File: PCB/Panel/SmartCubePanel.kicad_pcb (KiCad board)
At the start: 2 copper layers, 174.6 x 142.8 mm, 912 parts, among them J1 PogoPinPad, J1 SWD_Programmer, J1 Shield_Connector_Top_Left, J2 Conn_01x06, J2 Shield_Connector_Bottom_Left, J2 Shield_Connector_Top_Right, J3 PogoPinPad, J3 Shield_Connector_Bottom_Right, J3 Shield_Connector_Top_Right, J4 PogoPinPad, J4 Shield_Connector_Bottom_Right, J4 Shield_Connector_Top_Left, J5 Shield_Connector_Bottom_Left, U1 HallLinearSensor, U1 PY32F002BF15P6TU, U1 PogoPin, U2 PinHeaderTop, U2 PogoPin, U3 PinHeaderRight, U3 PogoPin, U4 PinHeaderBottom, U5 PinHeaderLeft

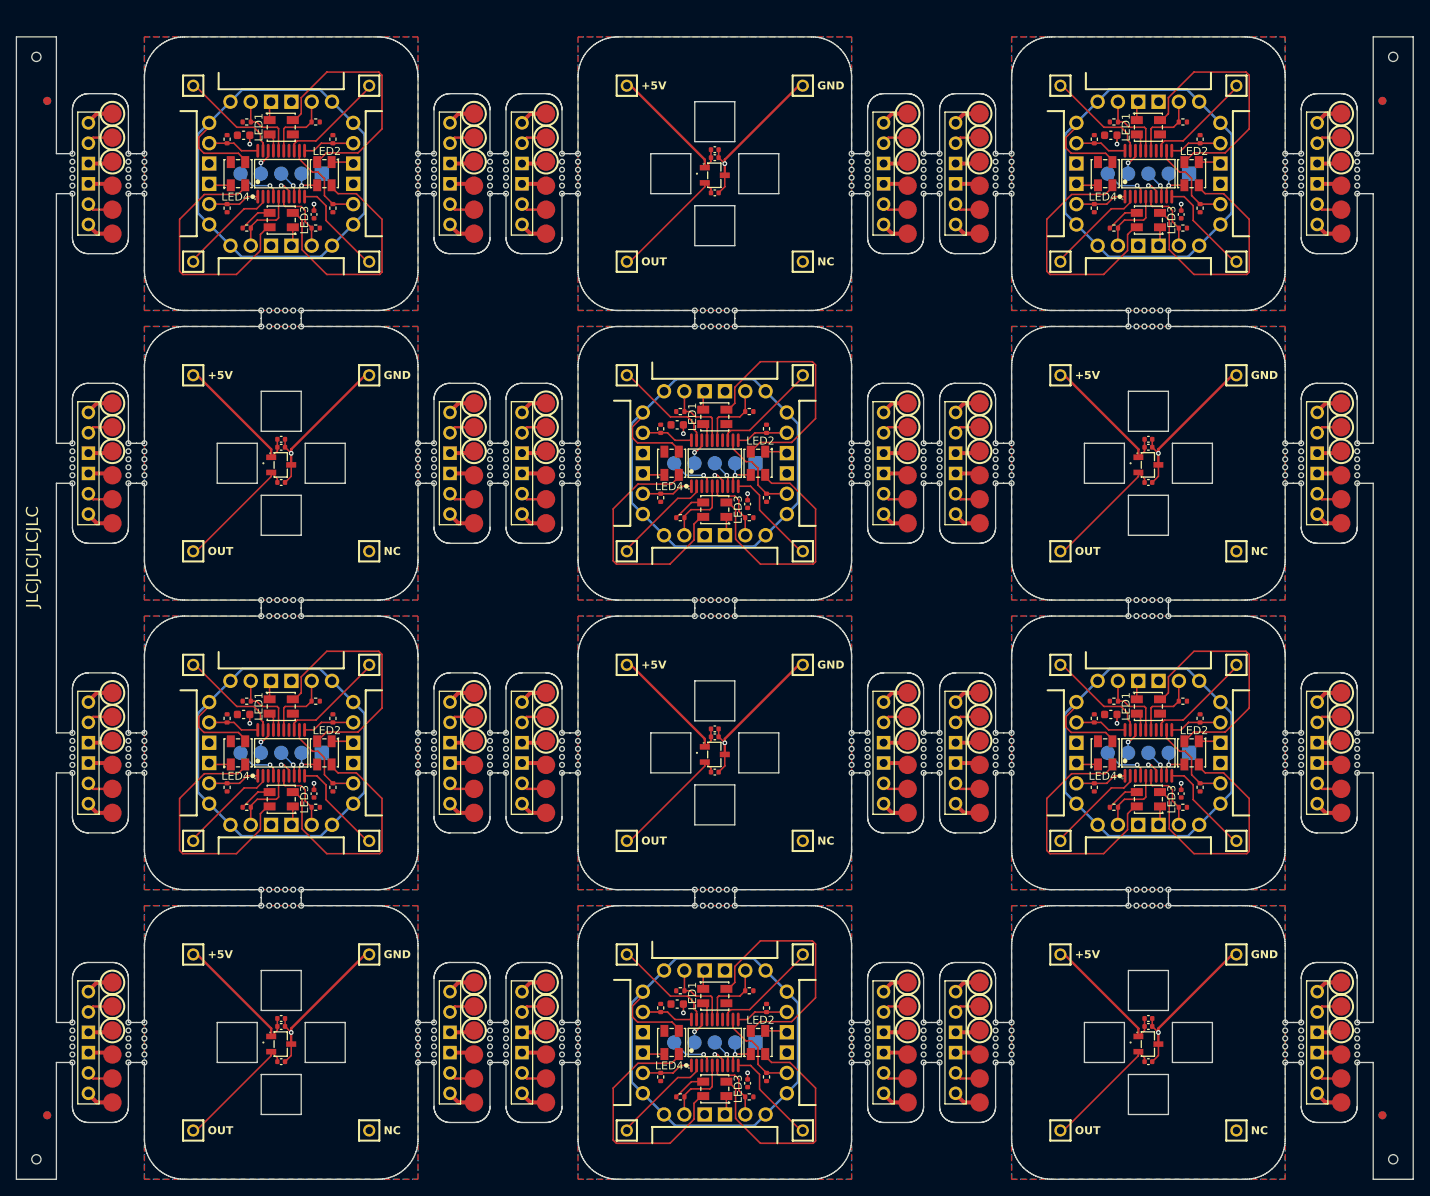
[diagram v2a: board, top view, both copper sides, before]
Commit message: Finish module, power supply and connector design, panel is wip
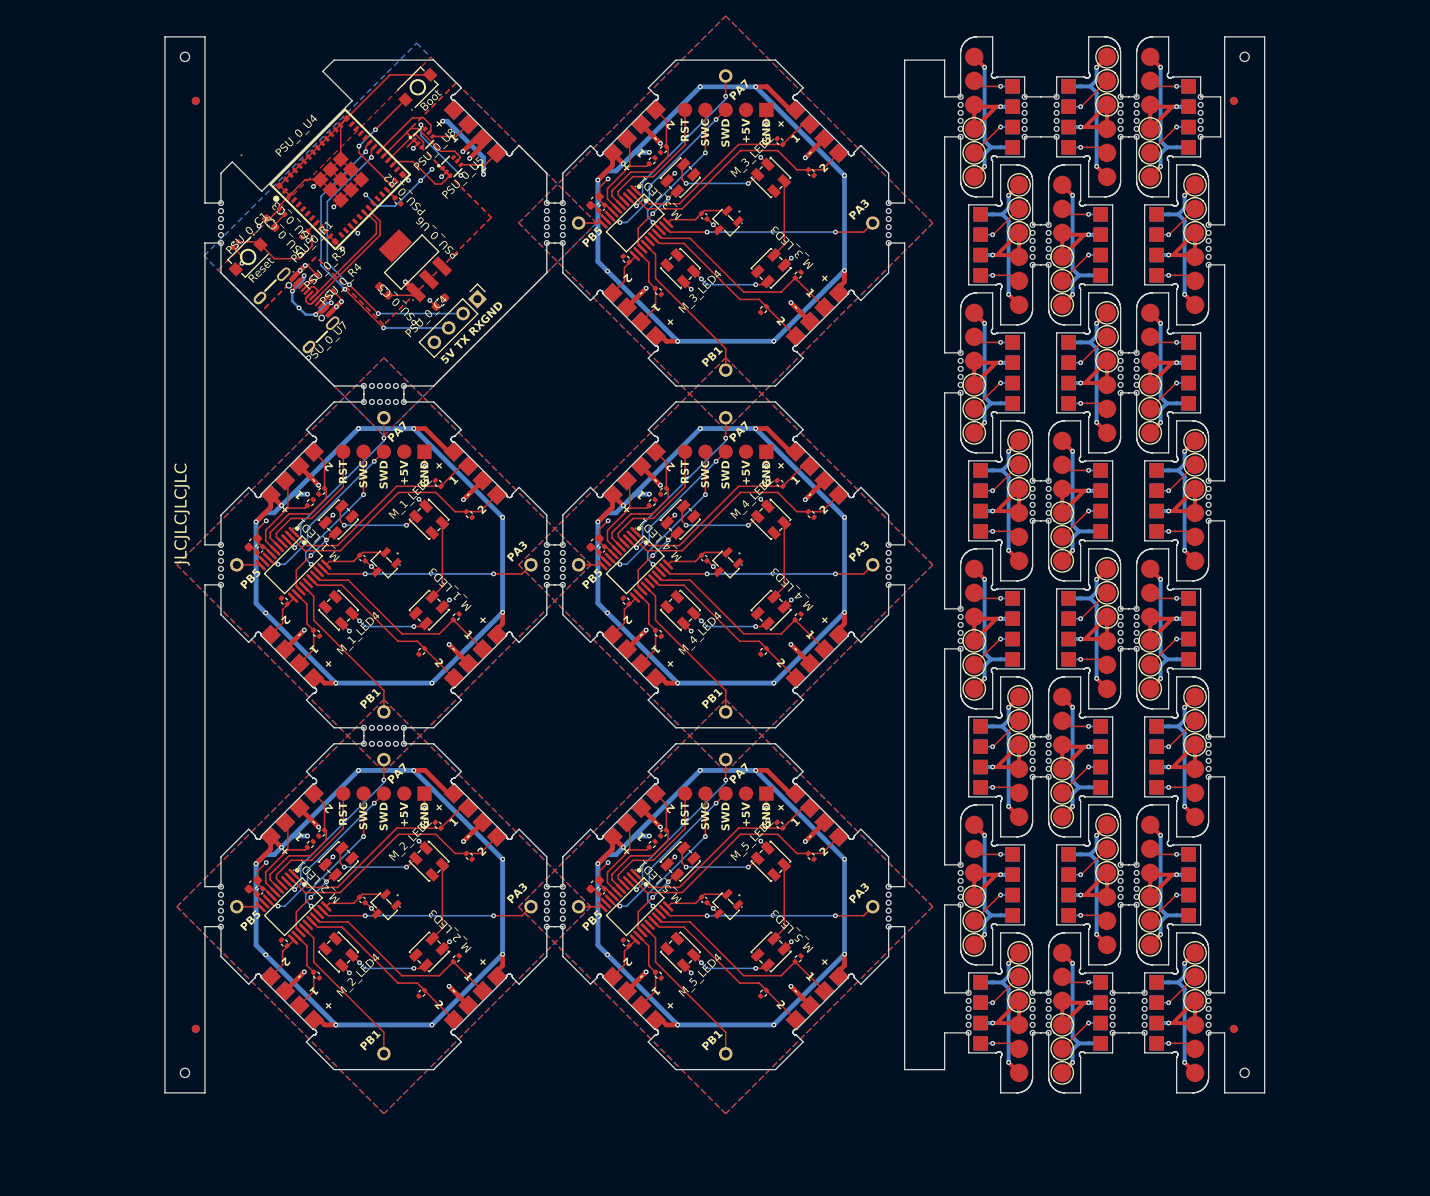
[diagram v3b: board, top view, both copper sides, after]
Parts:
- removed C1 (x6): 10nF, Capacitor_SMD:C_0402_1005Metric
- removed C1 (x6): 10uF, Capacitor_SMD:C_0603_1608Metric
- removed C2 (x6), C3 (x6): 1nF, Capacitor_SMD:C_0402_1005Metric
- removed C2 (x6): 100nF, Capacitor_SMD:C_0402_1005Metric
- removed J1 (x24), J3 (x24), J4 (x24): PogoPinPad, CustomFootprints:PogoPinPad
- removed J1 (x6), J4 (x6): Shield_Connector_Top_Left, CustomFootprints:HDR-TH_1P-V-F-1
- removed J1 (x6): SWD_Programmer, CustomFootprints:SWD_Pad
- removed J2 (x24): Conn_01x06, CustomFootprints:Connector_PinHeader_2.54mm_Vertical
- removed J2 (x6), J5 (x6): Shield_Connector_Bottom_Left, CustomFootprints:HDR-TH_1P-V-F-1
- removed J2 (x6), J3 (x6): Shield_Connector_Top_Right, CustomFootprints:HDR-TH_1P-V-F-1
- removed J3 (x6), J4 (x6): Shield_Connector_Bottom_Right, CustomFootprints:HDR-TH_1P-V-F-1
- removed KiKit_MB_47_1, KiKit_MB_47_2, KiKit_MB_47_3, KiKit_MB_47_4, KiKit_MB_47_5, KiKit_MB_47_6, KiKit_MB_48_1, KiKit_MB_48_2, KiKit_MB_48_3, KiKit_MB_48_4, KiKit_MB_48_5, KiKit_MB_48_6, KiKit_MB_49_1, KiKit_MB_49_2, KiKit_MB_49_3, KiKit_MB_49_4, KiKit_MB_49_5, KiKit_MB_49_6, KiKit_MB_50_1, KiKit_MB_50_2, KiKit_MB_50_3, KiKit_MB_50_4, KiKit_MB_50_5, KiKit_MB_50_6, KiKit_MB_51_1, KiKit_MB_51_2, KiKit_MB_51_3, KiKit_MB_51_4, KiKit_MB_51_5, KiKit_MB_51_6, KiKit_MB_52_1, KiKit_MB_52_2, KiKit_MB_52_3, KiKit_MB_52_4, KiKit_MB_52_5, KiKit_MB_52_6, KiKit_MB_53_1, KiKit_MB_53_2, KiKit_MB_53_3, KiKit_MB_53_4, KiKit_MB_53_5, KiKit_MB_53_6, KiKit_MB_54_1, KiKit_MB_54_2, KiKit_MB_54_3, KiKit_MB_54_4, KiKit_MB_54_5, KiKit_MB_54_6, KiKit_MB_55_1, KiKit_MB_55_2, KiKit_MB_55_3, KiKit_MB_55_4, KiKit_MB_55_5, KiKit_MB_55_6, KiKit_MB_56_1, KiKit_MB_56_2, KiKit_MB_56_3, KiKit_MB_56_4, KiKit_MB_56_5, KiKit_MB_56_6, KiKit_MB_57_1, KiKit_MB_57_2, KiKit_MB_57_3, KiKit_MB_57_4, KiKit_MB_57_5, KiKit_MB_57_6, KiKit_MB_58_1, KiKit_MB_58_2, KiKit_MB_58_3, KiKit_MB_58_4, KiKit_MB_58_5, KiKit_MB_58_6, KiKit_MB_59_1, KiKit_MB_59_2, KiKit_MB_59_3, KiKit_MB_59_4, KiKit_MB_59_5, KiKit_MB_59_6, KiKit_MB_60_1, KiKit_MB_60_2, KiKit_MB_60_3, KiKit_MB_60_4, KiKit_MB_60_5, KiKit_MB_60_6, KiKit_MB_61_1, KiKit_MB_61_2, KiKit_MB_61_3, KiKit_MB_61_4, KiKit_MB_61_5, KiKit_MB_61_6, KiKit_MB_62_1, KiKit_MB_62_2, KiKit_MB_62_3, KiKit_MB_62_4, KiKit_MB_62_5, KiKit_MB_62_6, KiKit_MB_63_1, KiKit_MB_63_2, KiKit_MB_63_3, KiKit_MB_63_4, KiKit_MB_63_5, KiKit_MB_63_6, KiKit_MB_64_1, KiKit_MB_64_2, KiKit_MB_64_3, KiKit_MB_64_4, KiKit_MB_64_5, KiKit_MB_64_6, KiKit_MB_65_1, KiKit_MB_65_2, KiKit_MB_65_3, KiKit_MB_65_4, KiKit_MB_65_5, KiKit_MB_65_6, KiKit_MB_66_1, KiKit_MB_66_2, KiKit_MB_66_3, KiKit_MB_66_4, KiKit_MB_66_5, KiKit_MB_66_6, KiKit_MB_67_1, KiKit_MB_67_2, KiKit_MB_67_3, KiKit_MB_67_4, KiKit_MB_67_5, KiKit_MB_67_6, KiKit_MB_68_1, KiKit_MB_68_2, KiKit_MB_68_3, KiKit_MB_68_4, KiKit_MB_68_5, KiKit_MB_68_6, KiKit_MB_69_1, KiKit_MB_69_2, KiKit_MB_69_3, KiKit_MB_69_4, KiKit_MB_69_5, KiKit_MB_69_6, KiKit_MB_70_1, KiKit_MB_70_2, KiKit_MB_70_3, KiKit_MB_70_4, KiKit_MB_70_5, KiKit_MB_70_6, KiKit_MB_71_1, KiKit_MB_71_2, KiKit_MB_71_3, KiKit_MB_71_4, KiKit_MB_71_5, KiKit_MB_71_6, KiKit_MB_72_1, KiKit_MB_72_2, KiKit_MB_72_3, KiKit_MB_72_4, KiKit_MB_72_5, KiKit_MB_72_6, KiKit_MB_73_1, KiKit_MB_73_2, KiKit_MB_73_3, KiKit_MB_73_4, KiKit_MB_73_5, KiKit_MB_73_6, KiKit_MB_74_1, KiKit_MB_74_2, KiKit_MB_74_3, KiKit_MB_74_4, KiKit_MB_74_5, KiKit_MB_74_6, KiKit_MB_75_1, KiKit_MB_75_2, KiKit_MB_75_3, KiKit_MB_75_4, KiKit_MB_75_5, KiKit_MB_75_6, KiKit_MB_76_1, KiKit_MB_76_2, KiKit_MB_76_3, KiKit_MB_76_4, KiKit_MB_76_5, KiKit_MB_76_6, KiKit_MB_77_1, KiKit_MB_77_2, KiKit_MB_77_3, KiKit_MB_77_4, KiKit_MB_77_5, KiKit_MB_77_6, KiKit_MB_78_1, KiKit_MB_78_2, KiKit_MB_78_3, KiKit_MB_78_4, KiKit_MB_78_5, KiKit_MB_78_6, KiKit_MB_79_1, KiKit_MB_79_2, KiKit_MB_79_3, KiKit_MB_79_4, KiKit_MB_79_5, KiKit_MB_79_6, KiKit_MB_80_1, KiKit_MB_80_2, KiKit_MB_80_3, KiKit_MB_80_4, KiKit_MB_80_5, KiKit_MB_80_6, KiKit_MB_81_1, KiKit_MB_81_2, KiKit_MB_81_3, KiKit_MB_81_4, KiKit_MB_81_5, KiKit_MB_81_6, KiKit_MB_82_1, KiKit_MB_82_2, KiKit_MB_82_3, KiKit_MB_82_4, KiKit_MB_82_5, KiKit_MB_82_6, KiKit_MB_83_1, KiKit_MB_83_2, KiKit_MB_83_3, KiKit_MB_83_4, KiKit_MB_83_5, KiKit_MB_83_6, KiKit_MB_84_1, KiKit_MB_84_2, KiKit_MB_84_3, KiKit_MB_84_4, KiKit_MB_84_5, KiKit_MB_84_6, KiKit_MB_85_1, KiKit_MB_85_2, KiKit_MB_85_3, KiKit_MB_85_4, KiKit_MB_85_5, KiKit_MB_85_6, KiKit_MB_86_1, KiKit_MB_86_2, KiKit_MB_86_3, KiKit_MB_86_4, KiKit_MB_86_5, KiKit_MB_86_6, KiKit_MB_87_1, KiKit_MB_87_2, KiKit_MB_87_3, KiKit_MB_87_4, KiKit_MB_87_5, KiKit_MB_87_6, KiKit_MB_88_1, KiKit_MB_88_2, KiKit_MB_88_3, KiKit_MB_88_4, KiKit_MB_88_5, KiKit_MB_88_6, KiKit_MB_89_1, KiKit_MB_89_2, KiKit_MB_89_3, KiKit_MB_89_4, KiKit_MB_89_5, KiKit_MB_89_6, KiKit_MB_90_1, KiKit_MB_90_2, KiKit_MB_90_3, KiKit_MB_90_4, KiKit_MB_90_5, KiKit_MB_90_6: NPTH, NPTH
- removed LED1 (x6), LED2 (x6), LED3 (x6), LED4 (x6): SK6812MINI-HS, CustomFootprints:LED-SK6812MINI-HS
- removed R1 (x6), R2 (x6), R3 (x6), R4 (x6), R5 (x6), R6 (x6), R7 (x6), R8 (x6): 10k, Resistor_SMD:R_0402_1005Metric
- removed U1 (x6): PY32F002BF15P6TU, CustomFootprints:Py32
- removed U1 (x24), U2 (x24), U3 (x24): PogoPin, CustomFootprints:PogoPin
- removed U1 (x6): HallLinearSensor, CustomFootprints:HallLinearSensor
- removed U2 (x6): PinHeaderTop, CustomFootprints:01x06_PinHeader_Angled
- removed U3 (x6): PinHeaderRight, CustomFootprints:01x06_PinHeader_Angled
- removed U4 (x6): PinHeaderBottom, CustomFootprints:01x06_PinHeader_Angled
- removed U5 (x6): PinHeaderLeft, CustomFootprints:01x06_PinHeader_Angled
- added M_1_C1: 10uF, Capacitor_SMD:C_0603_1608Metric, F.Cu at (90.8, 83.2)
- added M_1_C2: 100nF, Capacitor_SMD:C_0402_1005Metric, F.Cu at (91.6, 84.1)
- added M_1_C3: 10nF, Capacitor_SMD:C_0402_1005Metric, F.Cu at (104.4, 85.2)
- added M_1_J1: SWD_Programmer, CustomFootprints:SWD_Pad, F.Cu at (107.2, 71.9)
- added M_1_J2: Conn_01x01, CustomFootprints:ShieldConnector, F.Cu at (88.6, 86.1)
- added M_1_J3: Conn_01x01, CustomFootprints:ShieldConnector, F.Cu at (107.0, 104.5)
- added M_1_J4: Conn_01x01, CustomFootprints:ShieldConnector, F.Cu at (107.0, 67.8)
- added M_1_J5: Conn_01x01, CustomFootprints:ShieldConnector, F.Cu at (125.4, 86.1)
- added M_1_LED1: SK6812MINI-HS, CustomFootprints:LED-SK6812MINI-HS, F.Cu at (101.5, 80.3)
- added M_1_LED2: SK6812MINI-HS, CustomFootprints:LED-SK6812MINI-HS, F.Cu at (112.8, 80.3)
- added M_1_LED3: SK6812MINI-HS, CustomFootprints:LED-SK6812MINI-HS, F.Cu at (112.8, 91.7)
- added M_1_LED4: SK6812MINI-HS, CustomFootprints:LED-SK6812MINI-HS, F.Cu at (101.5, 91.7)
- added M_1_PinHeaderBottom1: PinHeader, CustomFootprints:01x04_PinPads, F.Cu at (118.6, 97.5)
- added M_1_PinHeaderLeft1: PinHeader, CustomFootprints:01x04_PinPads, F.Cu at (95.7, 97.5)
- added M_1_PinHeaderRight1: PinHeader, CustomFootprints:01x04_PinPads, F.Cu at (118.6, 74.5)
- added M_1_PinHeaderTop1: PinHeader, CustomFootprints:01x04_PinPads, F.Cu at (95.7, 74.5)
- added M_1_R1: 10k, Resistor_SMD:R_0402_1005Metric, F.Cu at (99.4, 76.8)
- added M_1_R2: 10k, Resistor_SMD:R_0402_1005Metric, F.Cu at (97.9, 78.2)
- added M_1_R3: 10k, Resistor_SMD:R_0402_1005Metric, F.Cu at (117.8, 79.7)
- added M_1_R4: 10k, Resistor_SMD:R_0402_1005Metric, F.Cu at (113.9, 75.8)
- added M_1_R5: 10k, Resistor_SMD:R_0402_1005Metric, F.Cu at (111.9, 96.8)
- added M_1_R6: 10k, Resistor_SMD:R_0402_1005Metric, F.Cu at (116.2, 92.5)
- added M_1_R7: 10k, Resistor_SMD:R_0402_1005Metric, F.Cu at (94.7, 90.5)
- added M_1_R8: 10k, Resistor_SMD:R_0402_1005Metric, F.Cu at (98.7, 94.6)
- added M_1_U1: PY32F002BF15P6TU, CustomFootprints:Py32, F.Cu at (95.8, 86.0)
- added M_1_U6: HallLinearSensor, CustomFootprints:HallLinearSensor, F.Cu at (107.1, 86.0)
- added M_2_C1: 10uF, Capacitor_SMD:C_0603_1608Metric, F.Cu at (90.8, 126.0)
- added M_2_C2: 100nF, Capacitor_SMD:C_0402_1005Metric, F.Cu at (91.6, 126.8)
- added M_2_C3: 10nF, Capacitor_SMD:C_0402_1005Metric, F.Cu at (104.4, 127.9)
- added M_2_J1: SWD_Programmer, CustomFootprints:SWD_Pad, F.Cu at (107.2, 114.6)
- added M_2_J2: Conn_01x01, CustomFootprints:ShieldConnector, F.Cu at (88.6, 128.9)
- added M_2_J3: Conn_01x01, CustomFootprints:ShieldConnector, F.Cu at (107.0, 147.3)
- added M_2_J4: Conn_01x01, CustomFootprints:ShieldConnector, F.Cu at (107.0, 110.5)
- added M_2_J5: Conn_01x01, CustomFootprints:ShieldConnector, F.Cu at (125.4, 128.9)
- added M_2_LED1: SK6812MINI-HS, CustomFootprints:LED-SK6812MINI-HS, F.Cu at (101.5, 123.1)
- added M_2_LED2: SK6812MINI-HS, CustomFootprints:LED-SK6812MINI-HS, F.Cu at (112.8, 123.1)
- added M_2_LED3: SK6812MINI-HS, CustomFootprints:LED-SK6812MINI-HS, F.Cu at (112.8, 134.4)
- added M_2_LED4: SK6812MINI-HS, CustomFootprints:LED-SK6812MINI-HS, F.Cu at (101.5, 134.4)
- added M_2_PinHeaderBottom1: PinHeader, CustomFootprints:01x04_PinPads, F.Cu at (118.6, 140.2)
- added M_2_PinHeaderLeft1: PinHeader, CustomFootprints:01x04_PinPads, F.Cu at (95.7, 140.2)
- added M_2_PinHeaderRight1: PinHeader, CustomFootprints:01x04_PinPads, F.Cu at (118.6, 117.3)
- added M_2_PinHeaderTop1: PinHeader, CustomFootprints:01x04_PinPads, F.Cu at (95.7, 117.3)
- added M_2_R1: 10k, Resistor_SMD:R_0402_1005Metric, F.Cu at (99.4, 119.5)
- added M_2_R2: 10k, Resistor_SMD:R_0402_1005Metric, F.Cu at (97.9, 121.0)
- added M_2_R3: 10k, Resistor_SMD:R_0402_1005Metric, F.Cu at (117.8, 122.4)
- added M_2_R4: 10k, Resistor_SMD:R_0402_1005Metric, F.Cu at (113.9, 118.5)
- added M_2_R5: 10k, Resistor_SMD:R_0402_1005Metric, F.Cu at (111.9, 139.5)
- added M_2_R6: 10k, Resistor_SMD:R_0402_1005Metric, F.Cu at (116.2, 135.2)
- added M_2_R7: 10k, Resistor_SMD:R_0402_1005Metric, F.Cu at (94.7, 133.3)
- added M_2_R8: 10k, Resistor_SMD:R_0402_1005Metric, F.Cu at (98.7, 137.3)
- added M_2_U1: PY32F002BF15P6TU, CustomFootprints:Py32, F.Cu at (95.8, 128.7)
- added M_2_U6: HallLinearSensor, CustomFootprints:HallLinearSensor, F.Cu at (107.1, 128.7)
- added M_3_C1: 10uF, Capacitor_SMD:C_0603_1608Metric, F.Cu at (133.5, 40.5)
- added M_3_C2: 100nF, Capacitor_SMD:C_0402_1005Metric, F.Cu at (134.4, 41.4)
- added M_3_C3: 10nF, Capacitor_SMD:C_0402_1005Metric, F.Cu at (147.2, 42.4)
- added M_3_J1: SWD_Programmer, CustomFootprints:SWD_Pad, F.Cu at (149.9, 29.1)
- added M_3_J2: Conn_01x01, CustomFootprints:ShieldConnector, F.Cu at (131.3, 43.4)
- added M_3_J3: Conn_01x01, CustomFootprints:ShieldConnector, F.Cu at (149.7, 61.8)
- added M_3_J4: Conn_01x01, CustomFootprints:ShieldConnector, F.Cu at (149.7, 25.0)
- added M_3_J5: Conn_01x01, CustomFootprints:ShieldConnector, F.Cu at (168.1, 43.4)
- added M_3_LED1: SK6812MINI-HS, CustomFootprints:LED-SK6812MINI-HS, F.Cu at (144.2, 37.6)
- added M_3_LED2: SK6812MINI-HS, CustomFootprints:LED-SK6812MINI-HS, F.Cu at (155.5, 37.6)
- added M_3_LED3: SK6812MINI-HS, CustomFootprints:LED-SK6812MINI-HS, F.Cu at (155.5, 48.9)
- added M_3_LED4: SK6812MINI-HS, CustomFootprints:LED-SK6812MINI-HS, F.Cu at (144.2, 48.9)
- added M_3_PinHeaderBottom1: PinHeader, CustomFootprints:01x04_PinPads, F.Cu at (161.3, 54.7)
- added M_3_PinHeaderLeft1: PinHeader, CustomFootprints:01x04_PinPads, F.Cu at (138.4, 54.7)
- added M_3_PinHeaderRight1: PinHeader, CustomFootprints:01x04_PinPads, F.Cu at (161.3, 31.8)
- added M_3_PinHeaderTop1: PinHeader, CustomFootprints:01x04_PinPads, F.Cu at (138.4, 31.8)
- added M_3_R1: 10k, Resistor_SMD:R_0402_1005Metric, F.Cu at (142.1, 34.1)
- added M_3_R2: 10k, Resistor_SMD:R_0402_1005Metric, F.Cu at (140.7, 35.5)
- added M_3_R3: 10k, Resistor_SMD:R_0402_1005Metric, F.Cu at (160.5, 37.0)
- added M_3_R4: 10k, Resistor_SMD:R_0402_1005Metric, F.Cu at (156.7, 33.1)
- added M_3_R5: 10k, Resistor_SMD:R_0402_1005Metric, F.Cu at (154.6, 54.1)
- added M_3_R6: 10k, Resistor_SMD:R_0402_1005Metric, F.Cu at (158.9, 49.8)
- added M_3_R7: 10k, Resistor_SMD:R_0402_1005Metric, F.Cu at (137.4, 47.8)
- added M_3_R8: 10k, Resistor_SMD:R_0402_1005Metric, F.Cu at (141.5, 51.8)
- added M_3_U1: PY32F002BF15P6TU, CustomFootprints:Py32, F.Cu at (138.6, 43.3)
- added M_3_U6: HallLinearSensor, CustomFootprints:HallLinearSensor, F.Cu at (149.9, 43.3)
- added M_4_C1: 10uF, Capacitor_SMD:C_0603_1608Metric, F.Cu at (133.5, 83.2)
- added M_4_C2: 100nF, Capacitor_SMD:C_0402_1005Metric, F.Cu at (134.4, 84.1)
- added M_4_C3: 10nF, Capacitor_SMD:C_0402_1005Metric, F.Cu at (147.2, 85.2)
- added M_4_J1: SWD_Programmer, CustomFootprints:SWD_Pad, F.Cu at (149.9, 71.9)
- added M_4_J2: Conn_01x01, CustomFootprints:ShieldConnector, F.Cu at (131.3, 86.1)
- added M_4_J3: Conn_01x01, CustomFootprints:ShieldConnector, F.Cu at (149.7, 104.5)
- added M_4_J4: Conn_01x01, CustomFootprints:ShieldConnector, F.Cu at (149.7, 67.8)
- added M_4_J5: Conn_01x01, CustomFootprints:ShieldConnector, F.Cu at (168.1, 86.1)
- added M_4_LED1: SK6812MINI-HS, CustomFootprints:LED-SK6812MINI-HS, F.Cu at (144.2, 80.3)
- added M_4_LED2: SK6812MINI-HS, CustomFootprints:LED-SK6812MINI-HS, F.Cu at (155.5, 80.3)
- added M_4_LED3: SK6812MINI-HS, CustomFootprints:LED-SK6812MINI-HS, F.Cu at (155.5, 91.7)
- added M_4_LED4: SK6812MINI-HS, CustomFootprints:LED-SK6812MINI-HS, F.Cu at (144.2, 91.7)
- added M_4_PinHeaderBottom1: PinHeader, CustomFootprints:01x04_PinPads, F.Cu at (161.3, 97.5)
- added M_4_PinHeaderLeft1: PinHeader, CustomFootprints:01x04_PinPads, F.Cu at (138.4, 97.5)
- added M_4_PinHeaderRight1: PinHeader, CustomFootprints:01x04_PinPads, F.Cu at (161.3, 74.5)
- added M_4_PinHeaderTop1: PinHeader, CustomFootprints:01x04_PinPads, F.Cu at (138.4, 74.5)
- added M_4_R1: 10k, Resistor_SMD:R_0402_1005Metric, F.Cu at (142.1, 76.8)
- added M_4_R2: 10k, Resistor_SMD:R_0402_1005Metric, F.Cu at (140.7, 78.2)
- added M_4_R3: 10k, Resistor_SMD:R_0402_1005Metric, F.Cu at (160.5, 79.7)
- added M_4_R4: 10k, Resistor_SMD:R_0402_1005Metric, F.Cu at (156.7, 75.8)
- added M_4_R5: 10k, Resistor_SMD:R_0402_1005Metric, F.Cu at (154.6, 96.8)
- added M_4_R6: 10k, Resistor_SMD:R_0402_1005Metric, F.Cu at (158.9, 92.5)
- added M_4_R7: 10k, Resistor_SMD:R_0402_1005Metric, F.Cu at (137.4, 90.5)
- added M_4_R8: 10k, Resistor_SMD:R_0402_1005Metric, F.Cu at (141.5, 94.6)
- added M_4_U1: PY32F002BF15P6TU, CustomFootprints:Py32, F.Cu at (138.6, 86.0)
- added M_4_U6: HallLinearSensor, CustomFootprints:HallLinearSensor, F.Cu at (149.9, 86.0)
- added M_5_C1: 10uF, Capacitor_SMD:C_0603_1608Metric, F.Cu at (133.5, 126.0)
- added M_5_C2: 100nF, Capacitor_SMD:C_0402_1005Metric, F.Cu at (134.4, 126.8)
- added M_5_C3: 10nF, Capacitor_SMD:C_0402_1005Metric, F.Cu at (147.2, 127.9)
- added M_5_J1: SWD_Programmer, CustomFootprints:SWD_Pad, F.Cu at (149.9, 114.6)
- added M_5_J2: Conn_01x01, CustomFootprints:ShieldConnector, F.Cu at (131.3, 128.9)
- added M_5_J3: Conn_01x01, CustomFootprints:ShieldConnector, F.Cu at (149.7, 147.3)
- added M_5_J4: Conn_01x01, CustomFootprints:ShieldConnector, F.Cu at (149.7, 110.5)
- added M_5_J5: Conn_01x01, CustomFootprints:ShieldConnector, F.Cu at (168.1, 128.9)
- added M_5_LED1: SK6812MINI-HS, CustomFootprints:LED-SK6812MINI-HS, F.Cu at (144.2, 123.1)
- added M_5_LED2: SK6812MINI-HS, CustomFootprints:LED-SK6812MINI-HS, F.Cu at (155.5, 123.1)
- added M_5_LED3: SK6812MINI-HS, CustomFootprints:LED-SK6812MINI-HS, F.Cu at (155.5, 134.4)
- added M_5_LED4: SK6812MINI-HS, CustomFootprints:LED-SK6812MINI-HS, F.Cu at (144.2, 134.4)
- added M_5_PinHeaderBottom1: PinHeader, CustomFootprints:01x04_PinPads, F.Cu at (161.3, 140.2)
- added M_5_PinHeaderLeft1: PinHeader, CustomFootprints:01x04_PinPads, F.Cu at (138.4, 140.2)
- added M_5_PinHeaderRight1: PinHeader, CustomFootprints:01x04_PinPads, F.Cu at (161.3, 117.3)
- added M_5_PinHeaderTop1: PinHeader, CustomFootprints:01x04_PinPads, F.Cu at (138.4, 117.3)
- added M_5_R1: 10k, Resistor_SMD:R_0402_1005Metric, F.Cu at (142.1, 119.5)
- added M_5_R2: 10k, Resistor_SMD:R_0402_1005Metric, F.Cu at (140.7, 121.0)
- added M_5_R3: 10k, Resistor_SMD:R_0402_1005Metric, F.Cu at (160.5, 122.4)
- added M_5_R4: 10k, Resistor_SMD:R_0402_1005Metric, F.Cu at (156.7, 118.5)
- added M_5_R5: 10k, Resistor_SMD:R_0402_1005Metric, F.Cu at (154.6, 139.5)
- added M_5_R6: 10k, Resistor_SMD:R_0402_1005Metric, F.Cu at (158.9, 135.2)
- added M_5_R7: 10k, Resistor_SMD:R_0402_1005Metric, F.Cu at (137.4, 133.3)
- added M_5_R8: 10k, Resistor_SMD:R_0402_1005Metric, F.Cu at (141.5, 137.3)
- added M_5_U1: PY32F002BF15P6TU, CustomFootprints:Py32, F.Cu at (138.6, 128.7)
- added M_5_U6: HallLinearSensor, CustomFootprints:HallLinearSensor, F.Cu at (149.9, 128.7)
- added POGO_10_J1: PogoPinPad, CustomFootprints:PogoPinPad, F.Cu at (180.9, 92.5)
- added POGO_10_J2: Conn_01x06, CustomFootprints:01x04_PinPads, B.Cu at (185.7, 94.0)
- added POGO_10_J3: PogoPinPad, CustomFootprints:PogoPinPad, F.Cu at (180.9, 89.5)
- added POGO_10_J4: PogoPinPad, CustomFootprints:PogoPinPad, F.Cu at (180.9, 86.5)
- added POGO_10_U1: PogoPin, CustomFootprints:PogoPin, F.Cu at (180.9, 101.5)
- added POGO_10_U2: PogoPin, CustomFootprints:PogoPin, F.Cu at (180.9, 98.5)
- added POGO_10_U3: PogoPin, CustomFootprints:PogoPin, F.Cu at (180.9, 95.5)
- added POGO_11_J1: PogoPinPad, CustomFootprints:PogoPinPad, F.Cu at (186.5, 111.5)
- added POGO_11_J2: Conn_01x06, CustomFootprints:01x04_PinPads, B.Cu at (181.7, 110.0)
- added POGO_11_J3: PogoPinPad, CustomFootprints:PogoPinPad, F.Cu at (186.5, 114.5)
- added POGO_11_J4: PogoPinPad, CustomFootprints:PogoPinPad, F.Cu at (186.5, 117.5)
- added POGO_11_U1: PogoPin, CustomFootprints:PogoPin, F.Cu at (186.5, 102.5)
- added POGO_11_U2: PogoPin, CustomFootprints:PogoPin, F.Cu at (186.5, 105.5)
- added POGO_11_U3: PogoPin, CustomFootprints:PogoPin, F.Cu at (186.5, 108.5)
- added POGO_12_J1: PogoPinPad, CustomFootprints:PogoPinPad, F.Cu at (180.9, 124.5)
- added POGO_12_J2: Conn_01x06, CustomFootprints:01x04_PinPads, B.Cu at (185.7, 126.0)
- added POGO_12_J3: PogoPinPad, CustomFootprints:PogoPinPad, F.Cu at (180.9, 121.5)
- added POGO_12_J4: PogoPinPad, CustomFootprints:PogoPinPad, F.Cu at (180.9, 118.5)
- added POGO_12_U1: PogoPin, CustomFootprints:PogoPin, F.Cu at (180.9, 133.5)
- added POGO_12_U2: PogoPin, CustomFootprints:PogoPin, F.Cu at (180.9, 130.5)
- added POGO_12_U3: PogoPin, CustomFootprints:PogoPin, F.Cu at (180.9, 127.5)
- added POGO_13_J1: PogoPinPad, CustomFootprints:PogoPinPad, F.Cu at (186.5, 143.5)
- added POGO_13_J2: Conn_01x06, CustomFootprints:01x04_PinPads, B.Cu at (181.7, 142.0)
- added POGO_13_J3: PogoPinPad, CustomFootprints:PogoPinPad, F.Cu at (186.5, 146.5)
- added POGO_13_J4: PogoPinPad, CustomFootprints:PogoPinPad, F.Cu at (186.5, 149.5)
- added POGO_13_U1: PogoPin, CustomFootprints:PogoPin, F.Cu at (186.5, 134.5)
- added POGO_13_U2: PogoPin, CustomFootprints:PogoPin, F.Cu at (186.5, 137.5)
- added POGO_13_U3: PogoPin, CustomFootprints:PogoPin, F.Cu at (186.5, 140.5)
- added POGO_14_J1: PogoPinPad, CustomFootprints:PogoPinPad, F.Cu at (197.5, 31.5)
- added POGO_14_J2: Conn_01x06, CustomFootprints:01x04_PinPads, B.Cu at (192.7, 30.0)
- added POGO_14_J3: PogoPinPad, CustomFootprints:PogoPinPad, F.Cu at (197.5, 34.5)
- added POGO_14_J4: PogoPinPad, CustomFootprints:PogoPinPad, F.Cu at (197.5, 37.5)
- added POGO_14_U1: PogoPin, CustomFootprints:PogoPin, F.Cu at (197.5, 22.5)
- added POGO_14_U2: PogoPin, CustomFootprints:PogoPin, F.Cu at (197.5, 25.5)
- added POGO_14_U3: PogoPin, CustomFootprints:PogoPin, F.Cu at (197.5, 28.5)
- added POGO_15_J1: PogoPinPad, CustomFootprints:PogoPinPad, F.Cu at (191.9, 44.5)
- added POGO_15_J2: Conn_01x06, CustomFootprints:01x04_PinPads, B.Cu at (196.7, 46.0)
- added POGO_15_J3: PogoPinPad, CustomFootprints:PogoPinPad, F.Cu at (191.9, 41.5)
- added POGO_15_J4: PogoPinPad, CustomFootprints:PogoPinPad, F.Cu at (191.9, 38.5)
- added POGO_15_U1: PogoPin, CustomFootprints:PogoPin, F.Cu at (191.9, 53.5)
- added POGO_15_U2: PogoPin, CustomFootprints:PogoPin, F.Cu at (191.9, 50.5)
- added POGO_15_U3: PogoPin, CustomFootprints:PogoPin, F.Cu at (191.9, 47.5)
- added POGO_16_J1: PogoPinPad, CustomFootprints:PogoPinPad, F.Cu at (197.5, 63.5)
- added POGO_16_J2: Conn_01x06, CustomFootprints:01x04_PinPads, B.Cu at (192.7, 62.0)
- added POGO_16_J3: PogoPinPad, CustomFootprints:PogoPinPad, F.Cu at (197.5, 66.5)
- added POGO_16_J4: PogoPinPad, CustomFootprints:PogoPinPad, F.Cu at (197.5, 69.5)
- added POGO_16_U1: PogoPin, CustomFootprints:PogoPin, F.Cu at (197.5, 54.5)
- added POGO_16_U2: PogoPin, CustomFootprints:PogoPin, F.Cu at (197.5, 57.5)
- added POGO_16_U3: PogoPin, CustomFootprints:PogoPin, F.Cu at (197.5, 60.5)
- added POGO_17_J1: PogoPinPad, CustomFootprints:PogoPinPad, F.Cu at (191.9, 76.5)
- added POGO_17_J2: Conn_01x06, CustomFootprints:01x04_PinPads, B.Cu at (196.7, 78.0)
- added POGO_17_J3: PogoPinPad, CustomFootprints:PogoPinPad, F.Cu at (191.9, 73.5)
- added POGO_17_J4: PogoPinPad, CustomFootprints:PogoPinPad, F.Cu at (191.9, 70.5)
- added POGO_17_U1: PogoPin, CustomFootprints:PogoPin, F.Cu at (191.9, 85.5)
- added POGO_17_U2: PogoPin, CustomFootprints:PogoPin, F.Cu at (191.9, 82.5)
- added POGO_17_U3: PogoPin, CustomFootprints:PogoPin, F.Cu at (191.9, 79.5)
- added POGO_18_J1: PogoPinPad, CustomFootprints:PogoPinPad, F.Cu at (197.5, 95.5)
- added POGO_18_J2: Conn_01x06, CustomFootprints:01x04_PinPads, B.Cu at (192.7, 94.0)
- added POGO_18_J3: PogoPinPad, CustomFootprints:PogoPinPad, F.Cu at (197.5, 98.5)
- added POGO_18_J4: PogoPinPad, CustomFootprints:PogoPinPad, F.Cu at (197.5, 101.5)
- added POGO_18_U1: PogoPin, CustomFootprints:PogoPin, F.Cu at (197.5, 86.5)
- added POGO_18_U2: PogoPin, CustomFootprints:PogoPin, F.Cu at (197.5, 89.5)
- added POGO_18_U3: PogoPin, CustomFootprints:PogoPin, F.Cu at (197.5, 92.5)
- added POGO_19_J1: PogoPinPad, CustomFootprints:PogoPinPad, F.Cu at (191.9, 108.5)
- added POGO_19_J2: Conn_01x06, CustomFootprints:01x04_PinPads, B.Cu at (196.7, 110.0)
- added POGO_19_J3: PogoPinPad, CustomFootprints:PogoPinPad, F.Cu at (191.9, 105.5)
- added POGO_19_J4: PogoPinPad, CustomFootprints:PogoPinPad, F.Cu at (191.9, 102.5)
- added POGO_19_U1: PogoPin, CustomFootprints:PogoPin, F.Cu at (191.9, 117.5)
- added POGO_19_U2: PogoPin, CustomFootprints:PogoPin, F.Cu at (191.9, 114.5)
- added POGO_19_U3: PogoPin, CustomFootprints:PogoPin, F.Cu at (191.9, 111.5)
- added POGO_20_J1: PogoPinPad, CustomFootprints:PogoPinPad, F.Cu at (197.5, 127.5)
- added POGO_20_J2: Conn_01x06, CustomFootprints:01x04_PinPads, B.Cu at (192.7, 126.0)
- added POGO_20_J3: PogoPinPad, CustomFootprints:PogoPinPad, F.Cu at (197.5, 130.5)
- added POGO_20_J4: PogoPinPad, CustomFootprints:PogoPinPad, F.Cu at (197.5, 133.5)
- added POGO_20_U1: PogoPin, CustomFootprints:PogoPin, F.Cu at (197.5, 118.5)
- added POGO_20_U2: PogoPin, CustomFootprints:PogoPin, F.Cu at (197.5, 121.5)
- added POGO_20_U3: PogoPin, CustomFootprints:PogoPin, F.Cu at (197.5, 124.5)
- added POGO_21_J1: PogoPinPad, CustomFootprints:PogoPinPad, F.Cu at (191.9, 140.5)
- added POGO_21_J2: Conn_01x06, CustomFootprints:01x04_PinPads, B.Cu at (196.7, 142.0)
- added POGO_21_J3: PogoPinPad, CustomFootprints:PogoPinPad, F.Cu at (191.9, 137.5)
- added POGO_21_J4: PogoPinPad, CustomFootprints:PogoPinPad, F.Cu at (191.9, 134.5)
- added POGO_21_U1: PogoPin, CustomFootprints:PogoPin, F.Cu at (191.9, 149.5)
- added POGO_21_U2: PogoPin, CustomFootprints:PogoPin, F.Cu at (191.9, 146.5)
- added POGO_21_U3: PogoPin, CustomFootprints:PogoPin, F.Cu at (191.9, 143.5)
- added POGO_22_J1: PogoPinPad, CustomFootprints:PogoPinPad, F.Cu at (202.9, 28.5)
- added POGO_22_J2: Conn_01x06, CustomFootprints:01x04_PinPads, B.Cu at (207.7, 30.0)
- added POGO_22_J3: PogoPinPad, CustomFootprints:PogoPinPad, F.Cu at (202.9, 25.5)
- added POGO_22_J4: PogoPinPad, CustomFootprints:PogoPinPad, F.Cu at (202.9, 22.5)
- added POGO_22_U1: PogoPin, CustomFootprints:PogoPin, F.Cu at (202.9, 37.5)
- added POGO_22_U2: PogoPin, CustomFootprints:PogoPin, F.Cu at (202.9, 34.5)
- added POGO_22_U3: PogoPin, CustomFootprints:PogoPin, F.Cu at (202.9, 31.5)
- added POGO_23_J1: PogoPinPad, CustomFootprints:PogoPinPad, F.Cu at (208.5, 47.5)
- added POGO_23_J2: Conn_01x06, CustomFootprints:01x04_PinPads, B.Cu at (203.7, 46.0)
- added POGO_23_J3: PogoPinPad, CustomFootprints:PogoPinPad, F.Cu at (208.5, 50.5)
- added POGO_23_J4: PogoPinPad, CustomFootprints:PogoPinPad, F.Cu at (208.5, 53.5)
- added POGO_23_U1: PogoPin, CustomFootprints:PogoPin, F.Cu at (208.5, 38.5)
- added POGO_23_U2: PogoPin, CustomFootprints:PogoPin, F.Cu at (208.5, 41.5)
- added POGO_23_U3: PogoPin, CustomFootprints:PogoPin, F.Cu at (208.5, 44.5)
- added POGO_24_J1: PogoPinPad, CustomFootprints:PogoPinPad, F.Cu at (202.9, 60.5)
- added POGO_24_J2: Conn_01x06, CustomFootprints:01x04_PinPads, B.Cu at (207.7, 62.0)
- added POGO_24_J3: PogoPinPad, CustomFootprints:PogoPinPad, F.Cu at (202.9, 57.5)
- added POGO_24_J4: PogoPinPad, CustomFootprints:PogoPinPad, F.Cu at (202.9, 54.5)
- added POGO_24_U1: PogoPin, CustomFootprints:PogoPin, F.Cu at (202.9, 69.5)
- added POGO_24_U2: PogoPin, CustomFootprints:PogoPin, F.Cu at (202.9, 66.5)
- added POGO_24_U3: PogoPin, CustomFootprints:PogoPin, F.Cu at (202.9, 63.5)
- added POGO_25_J1: PogoPinPad, CustomFootprints:PogoPinPad, F.Cu at (208.5, 79.5)
- added POGO_25_J2: Conn_01x06, CustomFootprints:01x04_PinPads, B.Cu at (203.7, 78.0)
- added POGO_25_J3: PogoPinPad, CustomFootprints:PogoPinPad, F.Cu at (208.5, 82.5)
- added POGO_25_J4: PogoPinPad, CustomFootprints:PogoPinPad, F.Cu at (208.5, 85.5)
- added POGO_25_U1: PogoPin, CustomFootprints:PogoPin, F.Cu at (208.5, 70.5)
- added POGO_25_U2: PogoPin, CustomFootprints:PogoPin, F.Cu at (208.5, 73.5)
- added POGO_25_U3: PogoPin, CustomFootprints:PogoPin, F.Cu at (208.5, 76.5)
- added POGO_26_J1: PogoPinPad, CustomFootprints:PogoPinPad, F.Cu at (202.9, 92.5)
- added POGO_26_J2: Conn_01x06, CustomFootprints:01x04_PinPads, B.Cu at (207.7, 94.0)
- added POGO_26_J3: PogoPinPad, CustomFootprints:PogoPinPad, F.Cu at (202.9, 89.5)
- added POGO_26_J4: PogoPinPad, CustomFootprints:PogoPinPad, F.Cu at (202.9, 86.5)
- added POGO_26_U1: PogoPin, CustomFootprints:PogoPin, F.Cu at (202.9, 101.5)
- added POGO_26_U2: PogoPin, CustomFootprints:PogoPin, F.Cu at (202.9, 98.5)
- added POGO_26_U3: PogoPin, CustomFootprints:PogoPin, F.Cu at (202.9, 95.5)
- added POGO_27_J1: PogoPinPad, CustomFootprints:PogoPinPad, F.Cu at (208.5, 111.5)
- added POGO_27_J2: Conn_01x06, CustomFootprints:01x04_PinPads, B.Cu at (203.7, 110.0)
- added POGO_27_J3: PogoPinPad, CustomFootprints:PogoPinPad, F.Cu at (208.5, 114.5)
- added POGO_27_J4: PogoPinPad, CustomFootprints:PogoPinPad, F.Cu at (208.5, 117.5)
- added POGO_27_U1: PogoPin, CustomFootprints:PogoPin, F.Cu at (208.5, 102.5)
- added POGO_27_U2: PogoPin, CustomFootprints:PogoPin, F.Cu at (208.5, 105.5)
- added POGO_27_U3: PogoPin, CustomFootprints:PogoPin, F.Cu at (208.5, 108.5)
- added POGO_28_J1: PogoPinPad, CustomFootprints:PogoPinPad, F.Cu at (202.9, 124.5)
- added POGO_28_J2: Conn_01x06, CustomFootprints:01x04_PinPads, B.Cu at (207.7, 126.0)
- added POGO_28_J3: PogoPinPad, CustomFootprints:PogoPinPad, F.Cu at (202.9, 121.5)
- added POGO_28_J4: PogoPinPad, CustomFootprints:PogoPinPad, F.Cu at (202.9, 118.5)
- added POGO_28_U1: PogoPin, CustomFootprints:PogoPin, F.Cu at (202.9, 133.5)
- added POGO_28_U2: PogoPin, CustomFootprints:PogoPin, F.Cu at (202.9, 130.5)
- added POGO_28_U3: PogoPin, CustomFootprints:PogoPin, F.Cu at (202.9, 127.5)
- added POGO_29_J1: PogoPinPad, CustomFootprints:PogoPinPad, F.Cu at (208.5, 143.5)
- added POGO_29_J2: Conn_01x06, CustomFootprints:01x04_PinPads, B.Cu at (203.7, 142.0)
- added POGO_29_J3: PogoPinPad, CustomFootprints:PogoPinPad, F.Cu at (208.5, 146.5)
- added POGO_29_J4: PogoPinPad, CustomFootprints:PogoPinPad, F.Cu at (208.5, 149.5)
- added POGO_29_U1: PogoPin, CustomFootprints:PogoPin, F.Cu at (208.5, 134.5)
- added POGO_29_U2: PogoPin, CustomFootprints:PogoPin, F.Cu at (208.5, 137.5)
- added POGO_29_U3: PogoPin, CustomFootprints:PogoPin, F.Cu at (208.5, 140.5)
- added POGO_6_J1: PogoPinPad, CustomFootprints:PogoPinPad, F.Cu at (180.9, 28.5)
- added POGO_6_J2: Conn_01x06, CustomFootprints:01x04_PinPads, B.Cu at (185.7, 30.0)
- added POGO_6_J3: PogoPinPad, CustomFootprints:PogoPinPad, F.Cu at (180.9, 25.5)
- added POGO_6_J4: PogoPinPad, CustomFootprints:PogoPinPad, F.Cu at (180.9, 22.5)
- added POGO_6_U1: PogoPin, CustomFootprints:PogoPin, F.Cu at (180.9, 37.5)
- added POGO_6_U2: PogoPin, CustomFootprints:PogoPin, F.Cu at (180.9, 34.5)
- added POGO_6_U3: PogoPin, CustomFootprints:PogoPin, F.Cu at (180.9, 31.5)
- added POGO_7_J1: PogoPinPad, CustomFootprints:PogoPinPad, F.Cu at (186.5, 47.5)
- added POGO_7_J2: Conn_01x06, CustomFootprints:01x04_PinPads, B.Cu at (181.7, 46.0)
- added POGO_7_J3: PogoPinPad, CustomFootprints:PogoPinPad, F.Cu at (186.5, 50.5)
- added POGO_7_J4: PogoPinPad, CustomFootprints:PogoPinPad, F.Cu at (186.5, 53.5)
- added POGO_7_U1: PogoPin, CustomFootprints:PogoPin, F.Cu at (186.5, 38.5)
- added POGO_7_U2: PogoPin, CustomFootprints:PogoPin, F.Cu at (186.5, 41.5)
- added POGO_7_U3: PogoPin, CustomFootprints:PogoPin, F.Cu at (186.5, 44.5)
- added POGO_8_J1: PogoPinPad, CustomFootprints:PogoPinPad, F.Cu at (180.9, 60.5)
- added POGO_8_J2: Conn_01x06, CustomFootprints:01x04_PinPads, B.Cu at (185.7, 62.0)
- added POGO_8_J3: PogoPinPad, CustomFootprints:PogoPinPad, F.Cu at (180.9, 57.5)
- added POGO_8_J4: PogoPinPad, CustomFootprints:PogoPinPad, F.Cu at (180.9, 54.5)
- added POGO_8_U1: PogoPin, CustomFootprints:PogoPin, F.Cu at (180.9, 69.5)
- added POGO_8_U2: PogoPin, CustomFootprints:PogoPin, F.Cu at (180.9, 66.5)
- added POGO_8_U3: PogoPin, CustomFootprints:PogoPin, F.Cu at (180.9, 63.5)
- added POGO_9_J1: PogoPinPad, CustomFootprints:PogoPinPad, F.Cu at (186.5, 79.5)
- added POGO_9_J2: Conn_01x06, CustomFootprints:01x04_PinPads, B.Cu at (181.7, 78.0)
- added POGO_9_J3: PogoPinPad, CustomFootprints:PogoPinPad, F.Cu at (186.5, 82.5)
- added POGO_9_J4: PogoPinPad, CustomFootprints:PogoPinPad, F.Cu at (186.5, 85.5)
- added POGO_9_U1: PogoPin, CustomFootprints:PogoPin, F.Cu at (186.5, 70.5)
- added POGO_9_U2: PogoPin, CustomFootprints:PogoPin, F.Cu at (186.5, 73.5)
- added POGO_9_U3: PogoPin, CustomFootprints:PogoPin, F.Cu at (186.5, 76.5)
- added PSU_0_C1: 100nF-Ceramic, Capacitor_SMD:C_0402_1005Metric, F.Cu at (88.6, 46.0)
- added PSU_0_C2: 10uF, Capacitor_SMD:C_0603_1608Metric, F.Cu at (93.0, 43.3)
- added PSU_0_C3: 10nF, Capacitor_SMD:C_0402_1005Metric, F.Cu at (94.4, 41.9)
- added PSU_0_C4: 10uF, Capacitor_SMD:C_0603_1608Metric, F.Cu at (114.2, 53.2)
- added PSU_0_C5: 10uF, Capacitor_SMD:C_0603_1608Metric, F.Cu at (107.1, 51.8)
- added PSU_0_J1: Conn_01x03, Connector_PinHeader_2.54mm:PinHeader_1x04_P2.54mm_Vertical, F.Cu at (118.8, 52.8)
- added PSU_0_R1: 10k, Resistor_SMD:R_0402_1005Metric, F.Cu at (97.2, 44.7)
- added PSU_0_R2: 10k, Resistor_SMD:R_0402_1005Metric, F.Cu at (108.9, 40.5)
- added PSU_0_R3: 5k1, Resistor_SMD:R_0402_1005Metric, F.Cu at (98.4, 50.1)
- added PSU_0_R4: 5k1, Resistor_SMD:R_0402_1005Metric, F.Cu at (100.4, 52.1)
- added PSU_0_U2: Tactile-Switch, CustomFootprints:Button, F.Cu at (90.2, 47.5)
- added PSU_0_U3: Tactile-Switch, CustomFootprints:Button, F.Cu at (111.4, 26.3)
- added PSU_0_U4: ESP32-C6-MINI-1-N4, CustomFootprints:ESP32C6-Mini-1-N4, F.Cu at (101.8, 37.9)
- added PSU_0_U5: BidirectionalLogicLevelShifter, CustomFootprints:BidirectionalLogicLevelConverter, F.Cu at (115.6, 36.2)
- added PSU_0_U6: LinearVoltageRegulator, CustomFootprints:VoltageRegulator, F.Cu at (110.7, 48.2)
- added PSU_0_U7: USB-TypeC, CustomFootprints:USB-C-SMD_TYPE-C-6PIN-2MD-073, F.Cu at (96.4, 54.0)
- added PSU_0_U8: BidirectionalLogicLevelShifter, CustomFootprints:BidirectionalLogicLevelConverter, F.Cu at (112.1, 32.7)
- added PSU_0_U9: PinHeaderRight, CustomFootprints:01x04_PinPads, F.Cu at (118.6, 31.8)
- moved KiKit_MB_43_6 162.0 mm to (210.2, 112.5)
- moved KiKit_MB_43_5 161.0 mm to (210.2, 111.5)
- moved KiKit_MB_43_4 160.1 mm to (210.2, 110.5)
- moved KiKit_MB_43_3 159.2 mm to (210.2, 109.5)
- moved KiKit_MB_43_2 158.3 mm to (210.2, 108.5)
- moved KiKit_MB_43_1 157.4 mm to (210.2, 107.5)
- moved KiKit_MB_44_1 157.2 mm to (201.2, 128.5)
- moved KiKit_MB_44_2 156.0 mm to (201.2, 127.5)
- moved KiKit_MB_44_3 154.8 mm to (201.2, 126.5)
- moved KiKit_MB_44_4 153.7 mm to (201.2, 125.5)
- moved KiKit_MB_44_5 152.5 mm to (201.2, 124.5)
- moved KiKit_MB_46_1 151.5 mm to (210.2, 139.5)
- moved KiKit_MB_46_2 151.5 mm to (210.2, 140.5)
- moved KiKit_MB_46_3 151.5 mm to (210.2, 141.5)
- moved KiKit_MB_46_4 151.5 mm to (210.2, 142.5)
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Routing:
- net Board_4-+5V: track 17.2 -> 123.4 mm, vias 0 -> 10
- net Board_1-+5V: track 17.2 -> 123.4 mm, vias 0 -> 10
- net Board_3-+5V: track 17.2 -> 123.4 mm, vias 0 -> 10
- net Board_0-GND: track 13.2 -> 95.5 mm, vias 3 -> 17
- net Board_7-+5V: track 90.2 -> 19.4 mm, vias 1 -> 2
- net Board_10-+5V: track 90.2 -> 19.4 mm, vias 1 -> 2
- net Board_8-+5V: track 90.2 -> 19.4 mm, vias 1 -> 2
- net Board_0-+5V: track 90.2 -> 33.3 mm, vias 1 -> 9
- net Board_0-TX: track 0.00 -> 37.1 mm, vias 0 -> 3
- net Board_0-RX: track 0.00 -> 36.5 mm, vias 0 -> 3
- net Board_2-+5V: track 90.2 -> 123.4 mm, vias 1 -> 10
- net Board_5-+5V: track 90.2 -> 123.4 mm, vias 1 -> 10
- net Board_0-Net-(LED3-DOUT): track 31.6 -> 0.00 mm
- net Board_7-Net-(LED3-DOUT): track 31.6 -> 0.00 mm
- net Board_8-Net-(LED3-DOUT): track 31.6 -> 0.00 mm
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- added copper zone on F.Cu, net Board_0-+3.3V
- removed copper zone on F.Cu, net Board_10-+5V
- removed copper zone on B.Cu, net Board_10-GND
- removed copper zone on F.Cu, net Board_11-+5V
- removed copper zone on B.Cu, net Board_11-GND
- removed copper zone on F.Cu, net Board_6-+5V
- removed copper zone on B.Cu, net Board_6-GND
- removed copper zone on F.Cu, net Board_7-+5V
- removed copper zone on B.Cu, net Board_7-GND
- removed copper zone on F.Cu, net Board_8-+5V
- removed copper zone on B.Cu, net Board_8-GND
- removed copper zone on F.Cu, net Board_9-+5V
- removed copper zone on B.Cu, net Board_9-GND
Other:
- board size 174.6 x 142.8 mm -> 137.5 x 132 mm
- board text added: "+"
- board text added: "-"
- board text added: "1"
- board text added: "2"
- board text added: "5V"
- board text added: "Boot"
- board text added: "D1"
- board text added: "D2"
- board text added: "PA3"
- board text added: "PA7"
- board text added: "PB1"
- board text added: "PB5"
- board text added: "Pogo"
- board text added: "RX"
- board text added: "Reset"
- board text added: "TX"
- board text removed: "NC"
- board text removed: "OUT"
